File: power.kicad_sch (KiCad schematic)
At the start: 1 part

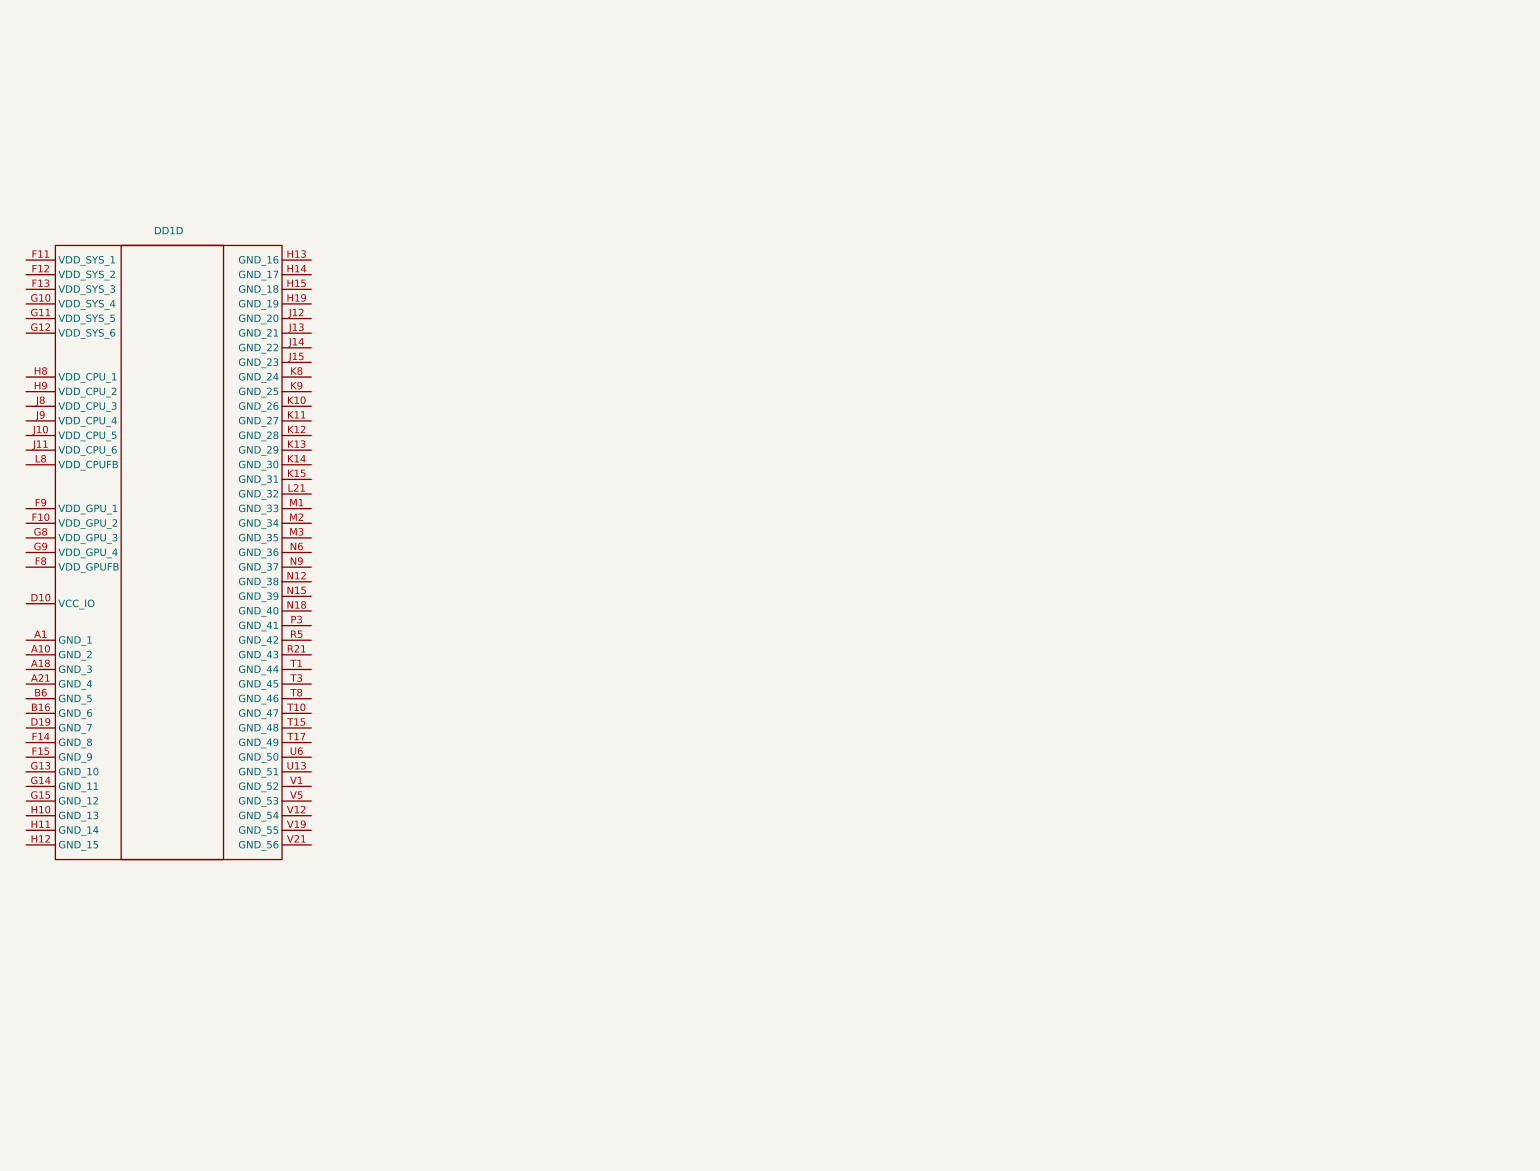
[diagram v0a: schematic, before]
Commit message: расставлены основные блоки и компоненты, подобраны компоненты интерфейса и питания
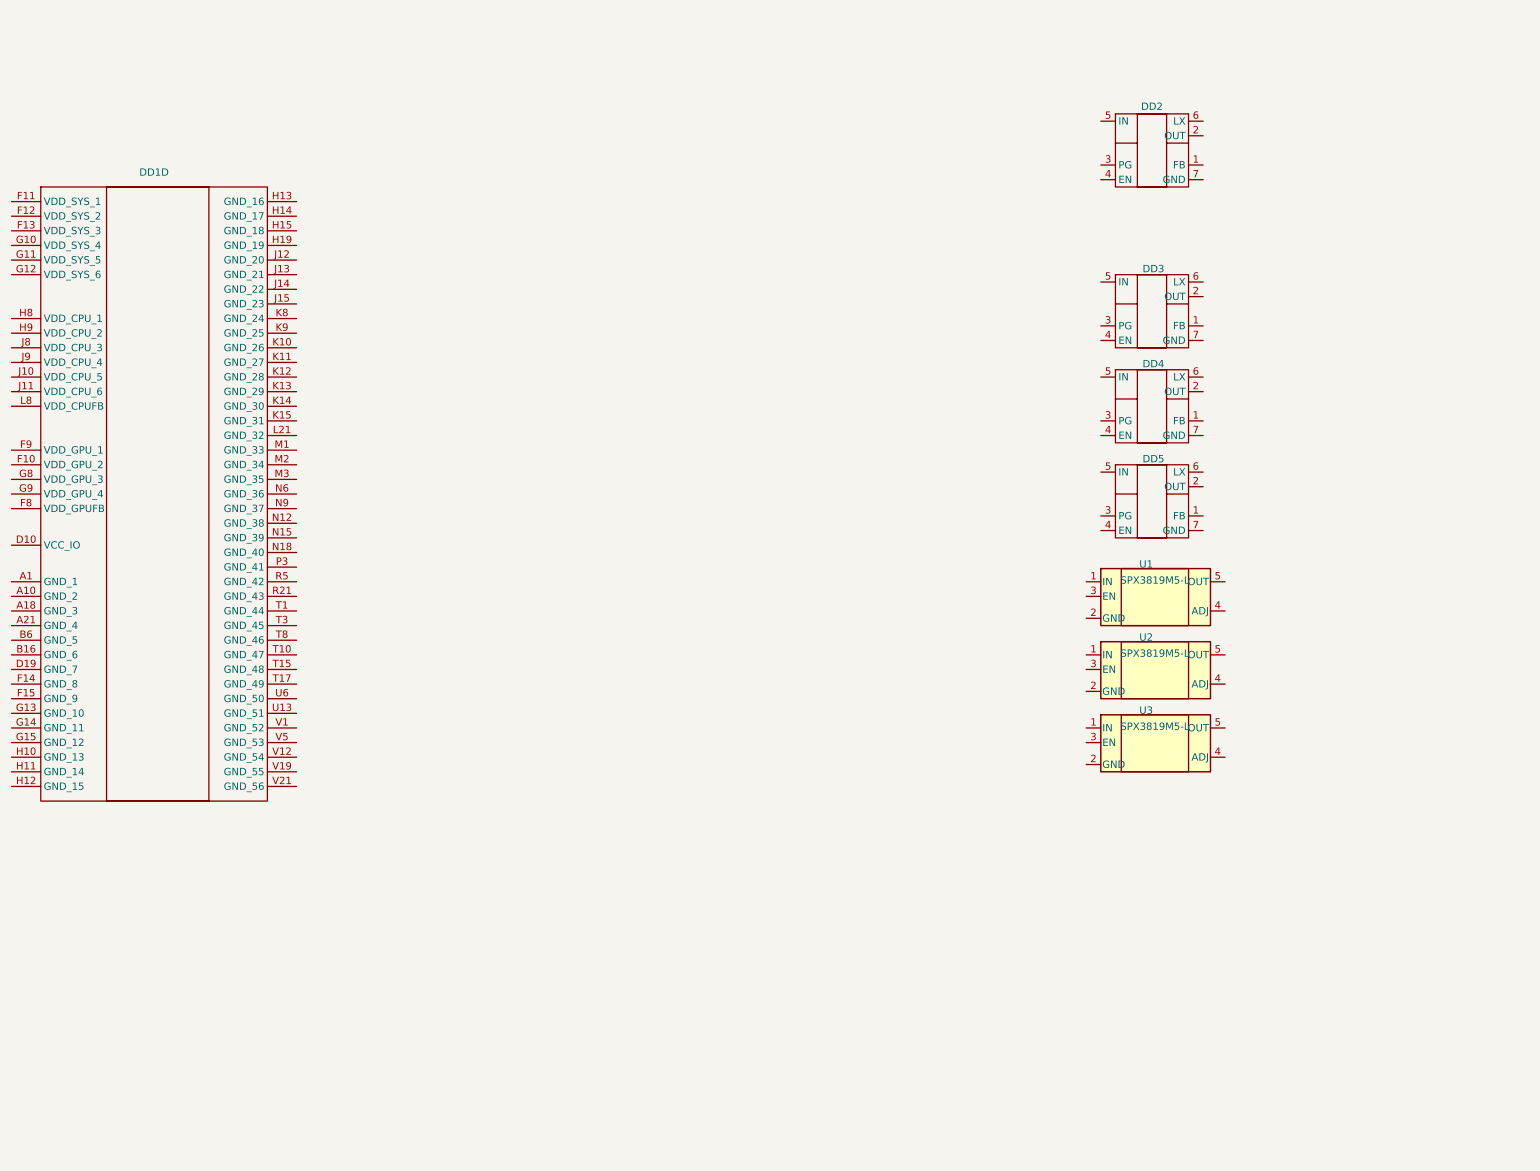
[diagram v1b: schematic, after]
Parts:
- added DD2, DD3, DD4, DD5: ~, SY8843QWC:SY8843QWC, symbol SY8843QWC:SY8843QWC
- added U1, U2, U3: SPX3819M5-L, Package_TO_SOT_SMD:SOT-23-5, symbol Regulator_Linear:SPX3819M5-L
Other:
- moved on the sheet: DD1D

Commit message: Доработка DDR, питание
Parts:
- removed DD3, DD4, DD5: ~, SY8843QWC:SY8843QWC, symbol SY8843QWC:SY8843QWC
- removed U3: SPX3819M5-L, Package_TO_SOT_SMD:SOT-23-5, symbol Regulator_Linear:SPX3819M5-L
- added C66, C71, C76: 100nF, Capacitor_SMD:C_0402_1005Metric, symbol Device:C
- added C69, C70, C72, C73, C74, C75: 22uF, Capacitor_SMD:C_0402_1005Metric, symbol Device:C
- added L1: 0.68uH, Inductor_SMD:L_APV_ANR4020, symbol Device:L
- added R18: 16.9К, Resistor_SMD:R_0402_1005Metric, symbol Device:R
- added R19: 10К, Resistor_SMD:R_0402_1005Metric, symbol Device:R
- added R20: 4.7К, Resistor_SMD:R_0402_1005Metric, symbol Device:R
- added R21: 10.2К, Resistor_SMD:R_0402_1005Metric, symbol Device:R
- added R22, R23: 0R, Resistor_SMD:R_0402_1005Metric, symbol Device:R
- added R24: 100К, Resistor_SMD:R_0402_1005Metric, symbol Device:R
- added R25: 49.9K, Resistor_SMD:R_0402_1005Metric, symbol Device:R
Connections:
- net at DD2.1 (FB): now also R24.1, R25.2
- net at DD2.2 (OUT): now also C75.1, C76.1, L1.2, R24.2
- net at DD2.6 (LX): now also L1.1
- net Earth: now reaches DD2.7 (GND)
- net Earth: now also C66.2, C69.2, C70.2, C71.2, C72.2, C73.2, C75.2, C76.2, R19.1, R21.1, R25.1
- net VCC-5V: now reaches U2.1 (IN)
- net VCC-5V: now also U1.1 (IN), C72.1, C73.1, R22.1, R23.1
- net at U2.3 (EN): now also R23.2
- net at U2.4 (ADJ): now also R20.1, R21.2
- net VCC18-ALDO: now reaches U2.5 (OUT)
- net VCC18-ALDO: now also C66.1, C69.1, R20.2
- net at U1.3 (EN): now also R22.2
- net at U1.4 (ADJ): now also R18.1, R19.2
- net VCC33-DLDO: now reaches U1.5 (OUT)
- net VCC33-DLDO: now also C70.1, C71.1, R18.2
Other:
- moved on the sheet: DD2, U1, U2

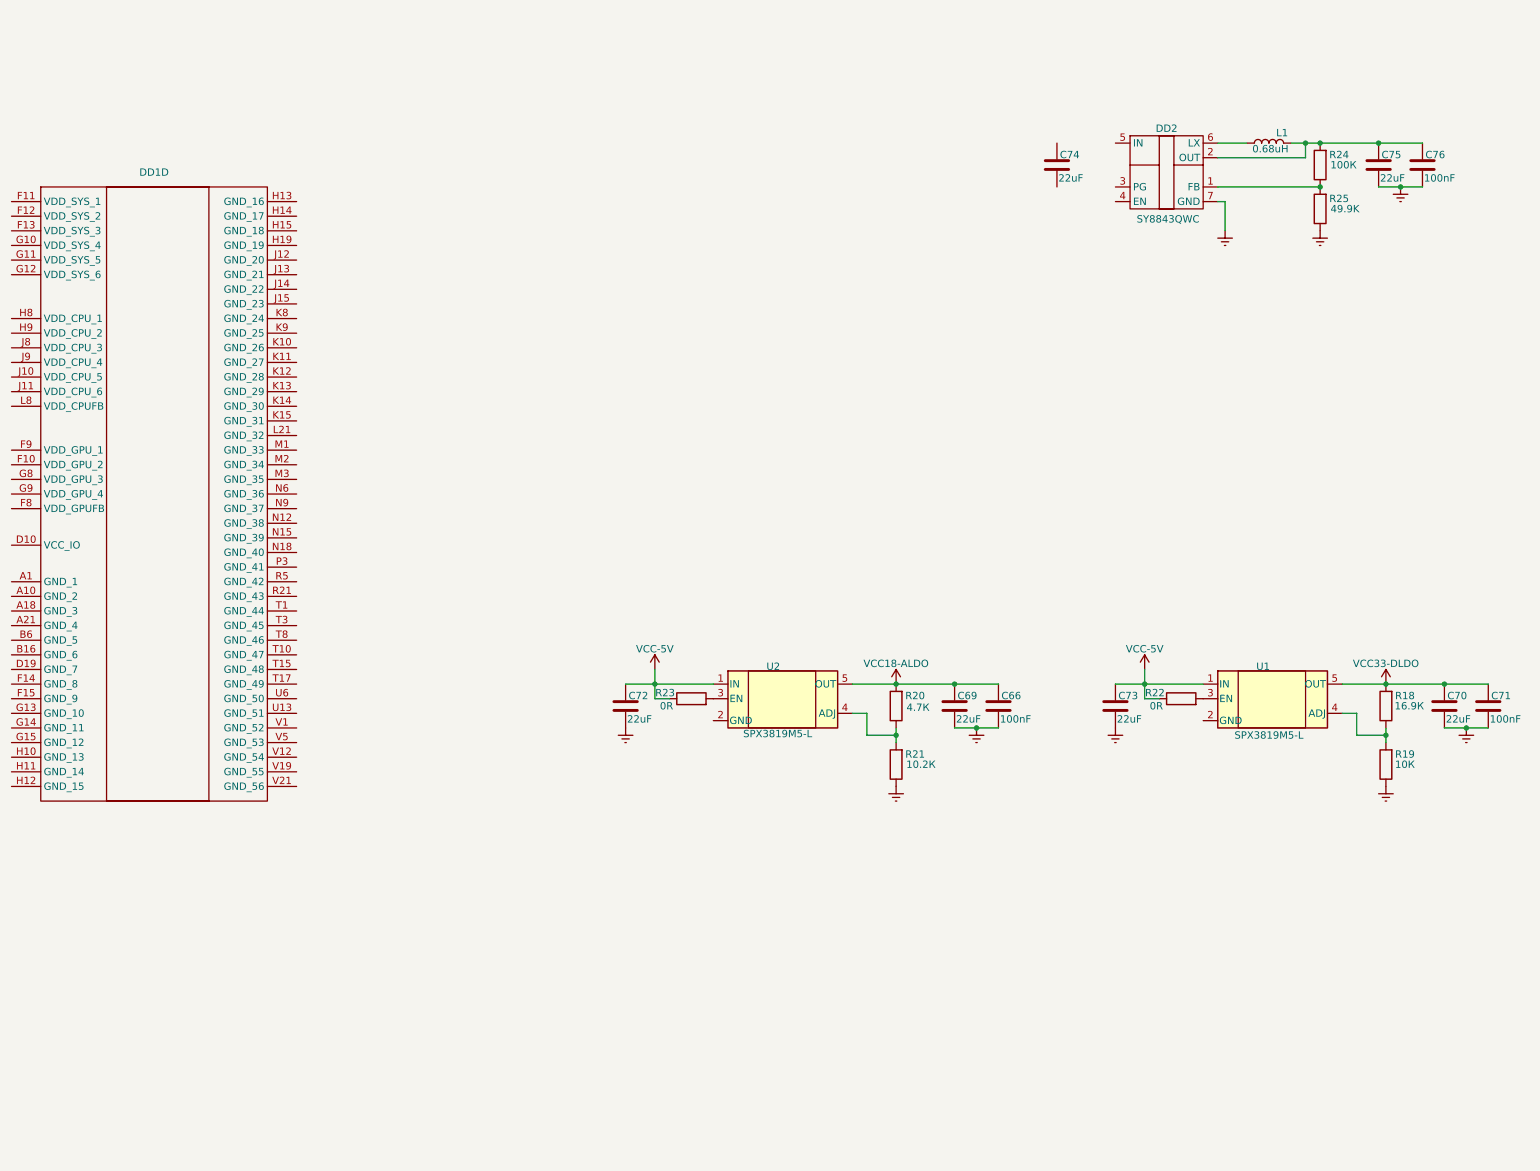
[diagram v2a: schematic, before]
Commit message: Обновлена структура, закончен интерфейс, HDMI Завершено проектирование линий питания и подтяжек для интерфейсов
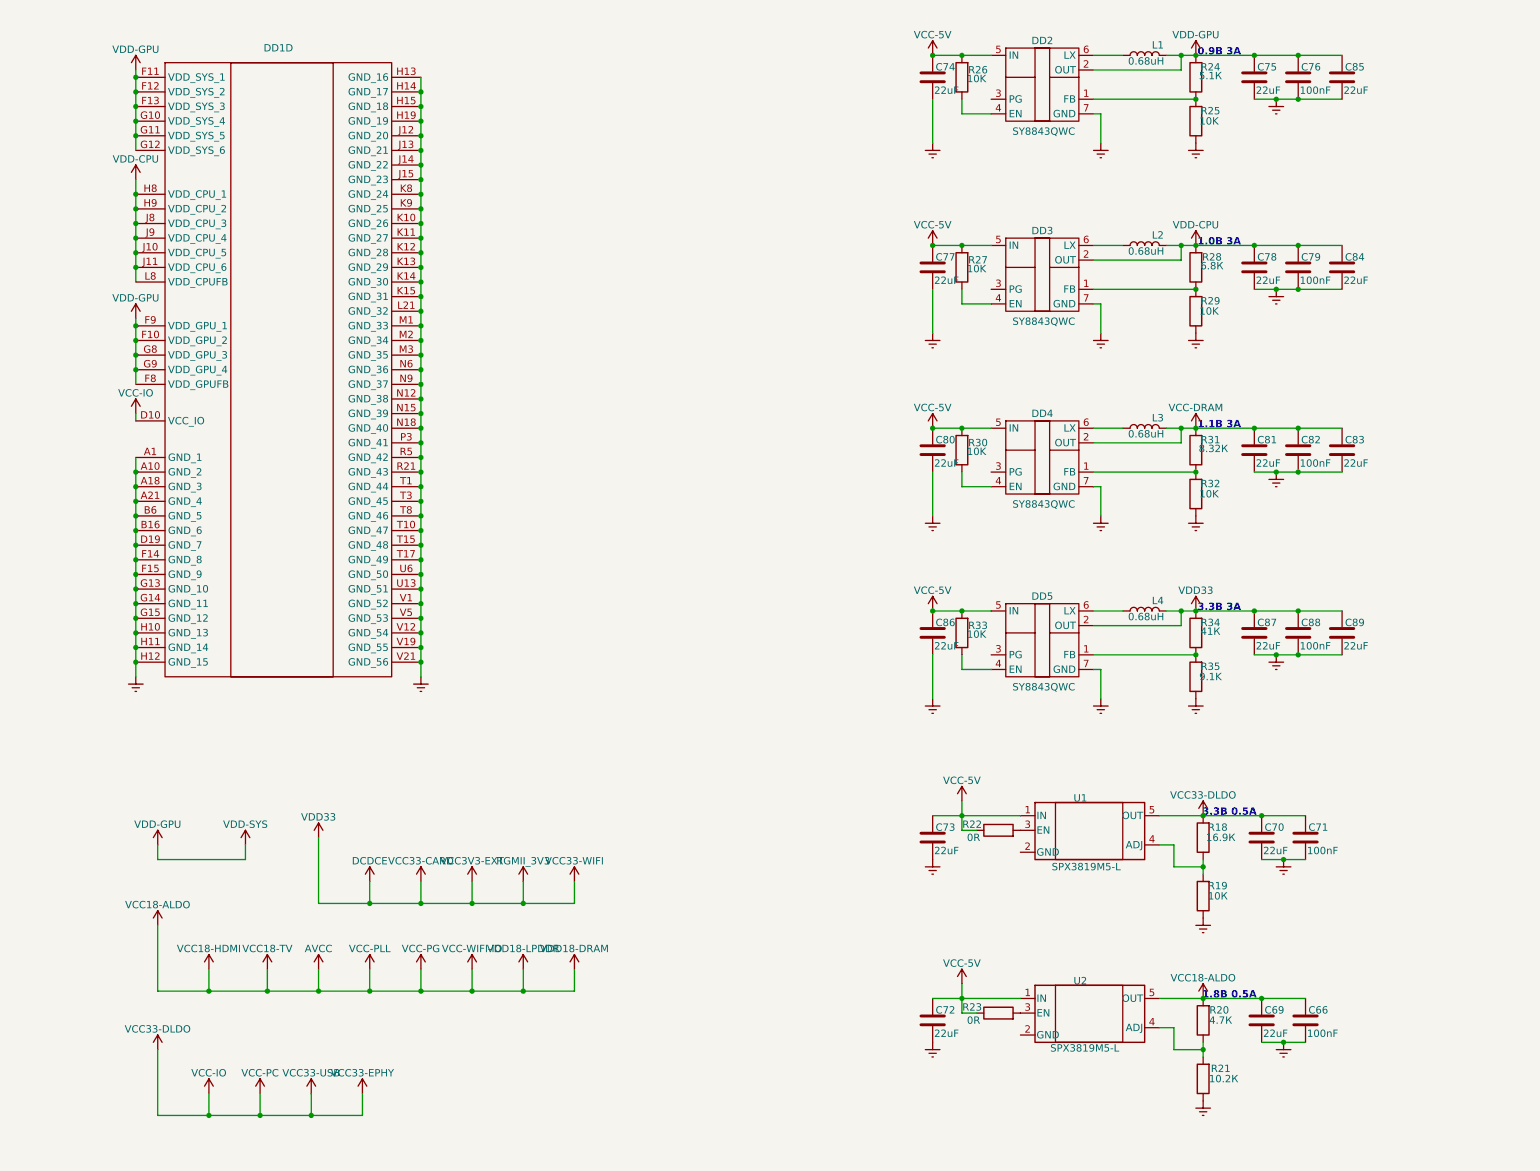
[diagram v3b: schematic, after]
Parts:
- added C77, C78, C80, C81, C83, C84, C85, C86, C87, C89: 22uF, Capacitor_SMD:C_0402_1005Metric, symbol Device:C
- added C79, C82, C88: 100nF, Capacitor_SMD:C_0402_1005Metric, symbol Device:C
- added DD3, DD4, DD5: ~, SY8843QWC:SY8843QWC, symbol SY8843QWC:SY8843QWC
- added L2, L3, L4: 0.68uH, Inductor_SMD:L_APV_ANR4020, symbol Device:L
- added R26, R27, R29, R30, R32, R33: 10K, Resistor_SMD:R_0402_1005Metric, symbol Device:R
- added R28: 6.8К, Resistor_SMD:R_0402_1005Metric, symbol Device:R
- added R31: 8.32К, Resistor_SMD:R_0402_1005Metric, symbol Device:R
- added R34: 41К, Resistor_SMD:R_0402_1005Metric, symbol Device:R
- added R35: 9.1K, Resistor_SMD:R_0402_1005Metric, symbol Device:R
- R24: value 100К -> 5.1К
- R25: value 49.9K -> 10K
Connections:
- net VCC33-DLDO is gone; now on net VCC-IO: C70.1, C71.1, R18.2, U1.5 (OUT)
- net Earth: now also C74.2, DD1.A1 (GND_1), DD1.A10 (GND_2), DD1.A18 (GND_3), DD1.A21 (GND_4), DD1.B16 (GND_6), DD1.B6 (GND_5), DD1.D19 (GND_7), DD1.F14 (GND_8), DD1.F15 (GND_9), DD1.G13 (GND_10), DD1.G14 (GND_11), DD1.G15 (GND_12), DD1.H10 (GND_13), DD1.H11 (GND_14), DD1.H12 (GND_15), DD1.H13 (GND_16), DD1.H14 (GND_17), DD1.H15 (GND_18), DD1.H19 (GND_19), DD1.J12 (GND_20), DD1.J13 (GND_21), DD1.J14 (GND_22), DD1.J15 (GND_23), DD1.K10 (GND_26), DD1.K11 (GND_27), DD1.K12 (GND_28), DD1.K13 (GND_29), DD1.K14 (GND_30), DD1.K15 (GND_31), DD1.K8 (GND_24), DD1.K9 (GND_25), DD1.L21 (GND_32), DD1.M1 (GND_33), DD1.M2 (GND_34), DD1.M3 (GND_35), DD1.N12 (GND_38), DD1.N15 (GND_39), DD1.N18 (GND_40), DD1.N6 (GND_36), DD1.N9 (GND_37), DD1.P3 (GND_41), DD1.R21 (GND_43), DD1.R5 (GND_42), DD1.T1 (GND_44), DD1.T10 (GND_47), DD1.T15 (GND_48), DD1.T17 (GND_49), DD1.T3 (GND_45), DD1.T8 (GND_46), DD1.U13 (GND_51), DD1.U6 (GND_50), DD1.V1 (GND_52), DD1.V12 (GND_54), DD1.V19 (GND_55), DD1.V21 (GND_56), DD1.V5 (GND_53), C77.2, C78.2, C79.2, C80.2, C81.2, C82.2, C83.2, C84.2, C85.2, C86.2, C87.2, C88.2, C89.2, DD3.7 (GND), DD4.7 (GND), DD5.7 (GND), R29.1, R32.1, R35.1
- net VCC-5V: now also C74.1, DD2.5 (IN), C77.1, C80.1, C86.1, DD3.5 (IN), DD4.5 (IN), DD5.5 (IN), R26.2, R27.2, R30.2, R33.2
- net VDD-GPU: now reaches C75.1, C76.1, DD2.2 (OUT), L1.2, R24.2
- net VDD-GPU: now also DD1.F10 (VDD_GPU_2), DD1.F11 (VDD_SYS_1), DD1.F12 (VDD_SYS_2), DD1.F13 (VDD_SYS_3), DD1.F8 (VDD_GPUFB), DD1.F9 (VDD_GPU_1), DD1.G10 (VDD_SYS_4), DD1.G11 (VDD_SYS_5), DD1.G12 (VDD_SYS_6), DD1.G8 (VDD_GPU_3), DD1.G9 (VDD_GPU_4), C85.1
- net at DD2.4 (EN): now also R26.1
- net VCC-IO: now reaches DD1.D10 (VCC_IO)
- net VDD-CPU: now reaches DD1.H8 (VDD_CPU_1)
- net VDD-CPU: now also DD1.H9 (VDD_CPU_2), DD1.J10 (VDD_CPU_5), DD1.J11 (VDD_CPU_6), DD1.J8 (VDD_CPU_3), DD1.J9 (VDD_CPU_4), DD1.L8 (VDD_CPUFB), C78.1, C79.1, C84.1, DD3.2 (OUT), L2.2, R28.2
- net VCC18-ALDO renamed AVCC
- new net: DD4.6 (LX), L3.1
- new net: DD4.1 (FB), R31.1, R32.2
- new net: DD4.4 (EN), R30.1
- new net: DD3.6 (LX), L2.1
- new net: DD3.1 (FB), R28.1, R29.2
- new net: DD5.1 (FB), R34.1, R35.2
- new net: DD3.4 (EN), R27.1
- new net: DD5.4 (EN), R33.1
- new net: DD5.6 (LX), L4.1
- new net DCDCE: C87.1, C88.1, C89.1, DD5.2 (OUT), L4.2, R34.2
- new net VCC-DRAM: C81.1, C82.1, C83.1, DD4.2 (OUT), L3.2, R31.2
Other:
- note added: "0.9В 3А"
- note added: "1.0В 3А"
- note added: "1.1В 3А"
- note added: "1.8В 0.5А"
- note added: "3.3В 0.5А"
- note added: "3.3В 3А"
- moved on the sheet: C66, C69, C70, C71, C72, C73, C74, C75, C76, DD1D, DD2, L1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

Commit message: Схема закончена, часть компонентов расставлена на плате
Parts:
- L1, L2, L3, L4: footprint Inductor_SMD:L_APV_ANR4020 -> Inductor_SMD:L_Cenker_CKCS4020
- renumbered C74 to C1, C87 to C10, C70 to C11, C69 to C12, C76 to C13, C79 to C14, C82 to C15, C88 to C16, C71 to C17, C66 to C18, C85 to C19, C77 to C2, C84 to C20, C83 to C21, C89 to C22, C80 to C3, C86 to C4, C73 to C5, C72 to C6, C75 to C7, C78 to C8, C81 to C9, R26 to R1, R29 to R10, R31 to R11, R32 to R12, R34 to R13, R35 to R14, R18 to R15, R19 to R16, R20 to R17, R21 to R18, R27 to R2, R30 to R3, R33 to R4, R22 to R5, R23 to R6, R24 to R7, R25 to R8, R28 to R9
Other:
- note added: "0.9V"
- note added: "1.0V"
- note added: "1.1V"
- note added: "1.8V"
- note added: "3.3V"
- note added: "CPU POWER"
- note added: "POWER DISTR"
- moved on the sheet: C12, C18, C6, R17, R18, R6, U2
